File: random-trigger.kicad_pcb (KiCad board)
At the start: 2 copper layers, 50.5 x 100 mm, 70 parts, among them J1 Eurorack Power, J10 Trigger Out B, J11 Inv Trigger Out B, J2 Noise In, J3 Noise Out, J4 Trigger In A, J5 Gate Out A, J6 Trigger Out A, J7 Inv Trigger Out A, J8 Trigger In B, J9 Gate Out B, Q1 2N3904, Q2 2N3904, U1 TL074, U2 LM7805_TO220, U3 4013, U4 4081

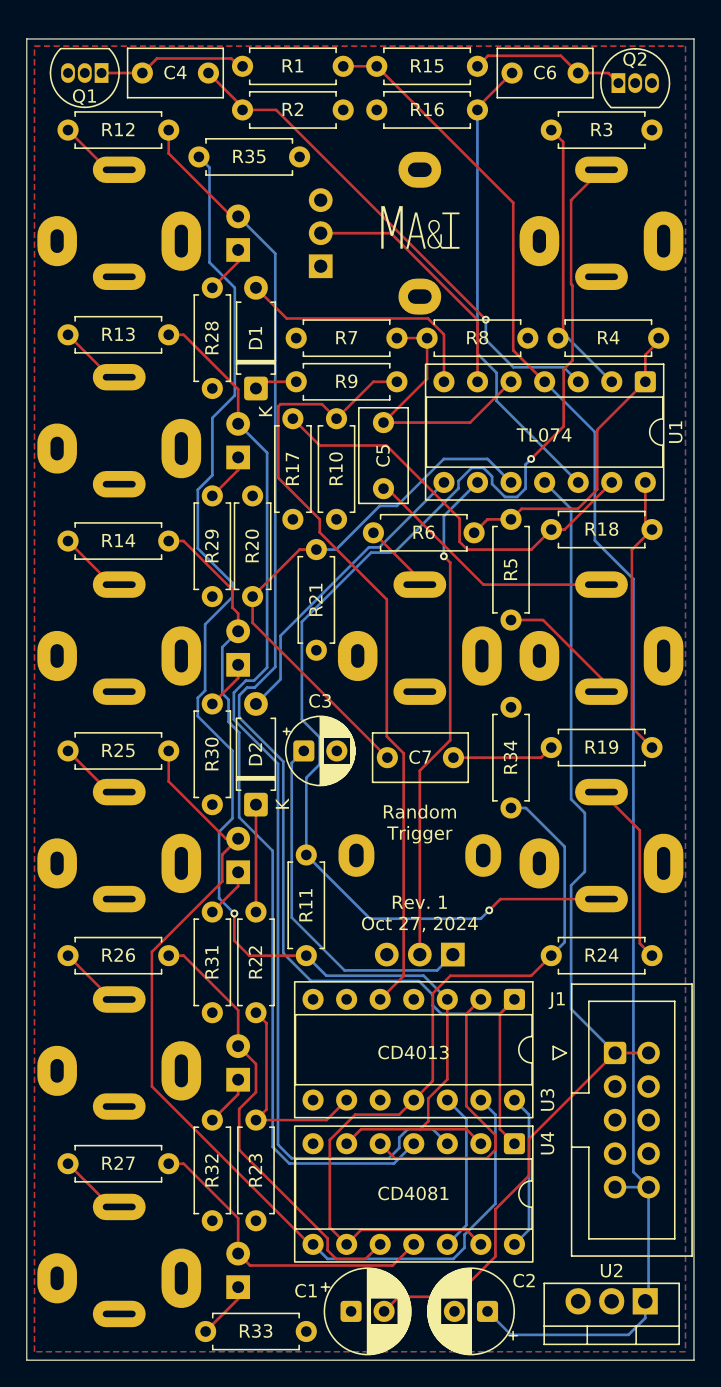
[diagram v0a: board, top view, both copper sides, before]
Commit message: Redo PCB to have all components on front
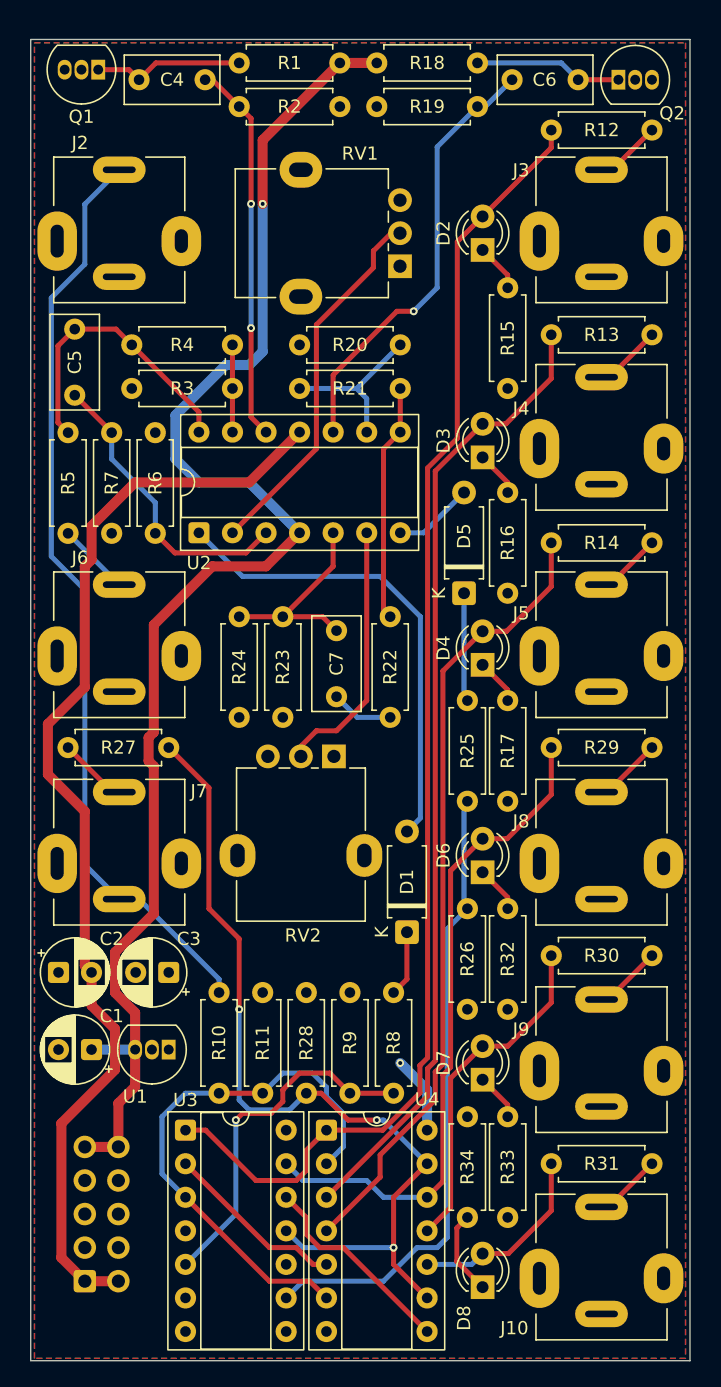
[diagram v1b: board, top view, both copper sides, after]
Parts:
- removed J11: Inv Trigger Out B, MAI_Connector_Audio:Jack_3.5mm_QingPu_WQP-PJ301BM_Vertical
- removed R35: 1M, Resistor_THT:R_Axial_DIN0207_L6.3mm_D2.5mm_P7.62mm_Horizontal
- removed the REF** at (129.8, 64.3)
- added REF**: Untitled, MAI_Logo:MAI_Logo_10mm_Silkscreen, B.Cu at (125.2, 83.6)
- C1, C2: footprint Capacitor_THT:CP_Radial_D6.3mm_P2.50mm -> Capacitor_THT:CP_Radial_D5.0mm_P2.50mm
- D2: value 1n4001 -> LED; footprint Diode_THT:D_A-405_P7.62mm_Horizontal -> LED_THT:LED_D3.0mm
- D3, D4, D6, D7, D8, RV1, RV2: moved to F.Cu
- D5: value LED -> 1n4001; footprint LED_THT:LED_D3.0mm -> Diode_THT:D_A-405_P7.62mm_Horizontal; moved to F.Cu
- J1: moved to B.Cu
- J10: value Trigger Out B -> Inv Trigger Out B; moved to F.Cu
- J2: value Noise In -> Trigger In A; moved to F.Cu
- J3: value Noise Out -> Gate Out A; moved to F.Cu
- J4: value Trigger In A -> Trigger Out A; moved to F.Cu
- J5: value Gate Out A -> Inv Trigger Out A; moved to F.Cu
- J6: value Trigger Out A -> Noise Out; moved to F.Cu
- J7: value Inv Trigger Out A -> Trigger In B; moved to F.Cu
- J8: value Trigger In B -> Gate Out B; moved to F.Cu
- J9: value Gate Out B -> Trigger Out B; moved to F.Cu
- R10, R22: value 1k5 -> 1k
- R11, R28: value 1k -> 1M
- R15, R16: value 100k -> 1k
- R17: value 330 -> 1k
- R18: value 1M -> 100k
- R19, R24, R6: value 1k -> 100k
- R20: value 100k -> 330
- R21: value 100k -> 1M
- R23: value 1k5 -> 100k
- R25, R26: value 1k -> 1k5
- R34: value 1M -> 1k
- R8: value 100k -> 1k5
- U1: value TL074 -> L78L05_TO92; footprint Package_DIP:DIP-14_W7.62mm_Socket -> Package_TO_SOT_THT:TO-92_Inline
- U2: value LM7805_TO220 -> TL074; footprint Package_TO_SOT_THT:TO-220-3_Vertical -> MAI_Package_DIP:DIP-14_W7.62mm_Socket_WithChip
- U3, U4: footprint Package_DIP:DIP-14_W7.62mm_Socket -> MAI_Package_DIP:DIP-14_W7.62mm_Socket_WithChip
- moved U2 67.3 mm to (113.0, 87.4), turned to 90 degrees
- moved U1 62.1 mm to (110.7, 126.5), turned to 180 degrees
- moved R28 61.4 mm to (121.2, 129.8), turned to 90 degrees
- moved R19 50.3 mm to (134.1, 55.1)
- moved R8 49.6 mm to (127.8, 122.2), turned to -90 degrees
- moved J2 48.1 mm to (107.0, 64.7), turned to 0 degrees
- moved J5 48.1 mm to (143.5, 96.1), turned to 0 degrees
- moved R9 46.4 mm to (124.5, 122.2), turned to -90 degrees
- moved D2 45.3 mm to (134.5, 66.0)
- moved R10 44.3 mm to (114.6, 129.8)
- moved J1 43.7 mm to (104.4, 144.0)
- moved D1 42.7 mm to (128.8, 117.6)
- moved C2 41.4 mm to (102.4, 120.7), turned to 0 degrees
- moved J9 39.7 mm to (143.5, 127.5), turned to 0 degrees
- moved J10 39.7 mm to (143.5, 143.2), turned to 0 degrees
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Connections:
- C1 pad 1: GND -> +12V
- C1 pad 2: -12V -> GND
- C2 pad 1: +12V -> GND
- C2 pad 2: GND -> -12V
- C4 pad 2: Net-(U1A-+) -> Net-(U2D-+)
- C5 pad 2: Net-(U1B-+) -> Net-(U2A-+)
- C6 pad 2: Net-(U1D-+) -> Net-(U2C-+)
- C7 pad 2: Net-(U1C-+) -> Net-(U2B-+)
- J2 pad T: Net-(C5-Pad1) -> Trigger Normal
- J2 pad TN: Net-(J2-PadTN) -> unconnected-(J2-PadTN)
- J4 pad T: Trigger Normal -> Net-(J4-PadT)
- J7 pad TN: unconnected-(J7-PadTN) -> Trigger Normal
- J8 pad TN: Trigger Normal -> unconnected-(J8-PadTN)
- R10 pad 1: GND -> Net-(U3A-C)
- R10 pad 2: Net-(U3A-D) -> Trigger Normal
- R11 pad 2: Trigger Normal -> GND
- R12 pad 1: Net-(D3-A) -> Net-(D2-A)
- R12 pad 2: Net-(J5-PadT) -> Net-(J3-PadT)
- R13 pad 1: Net-(D4-A) -> Net-(D3-A)
- R13 pad 2: Net-(J6-PadT) -> Net-(J4-PadT)
- R14 pad 1: Net-(D5-A) -> Net-(D4-A)
- R14 pad 2: Net-(J7-PadT) -> Net-(J5-PadT)
- R15 pad 1: +12V -> Net-(D2-K)
- R15 pad 2: Net-(Q2-E) -> GND
- R16 pad 1: Net-(U1D-+) -> Net-(D3-K)
- R17 pad 1: Net-(U1D--) -> Net-(D4-K)
- R18 pad 1: Net-(U1D--) -> +12V
- R18 pad 2: Net-(R18-Pad2) -> Net-(Q2-E)
- R19 pad 1: Net-(R18-Pad2) -> Net-(U2C-+)
- R19 pad 2: Net-(C7-Pad1) -> GND
- R2 pad 1: Net-(U1A-+) -> Net-(U2D-+)
- R20 pad 1: +5V -> Net-(U2C--)
- R20 pad 2: Net-(U1C-+) -> GND
- R21 pad 1: Net-(U1C-+) -> Net-(U2C--)
- R21 pad 2: GND -> Net-(R21-Pad2)
- R22 pad 1: Net-(D2-K) -> Net-(R21-Pad2)
- R22 pad 2: Net-(U3B-D) -> Net-(C7-Pad1)
- R23 pad 1: GND -> +5V
- R23 pad 2: Net-(U3B-D) -> Net-(U2B-+)
- R24 pad 1: Net-(U3B-C) -> Net-(U2B-+)
- R24 pad 2: Net-(J8-PadT) -> GND
- R25 pad 1: Net-(D6-A) -> Net-(D5-K)
- R25 pad 2: Net-(J9-PadT) -> Net-(U3B-D)
- R26 pad 1: Net-(D7-A) -> GND
- R26 pad 2: Net-(J10-PadT) -> Net-(U3B-D)
- R27 pad 1: Net-(D8-A) -> Net-(U3B-C)
- R27 pad 2: Net-(J11-PadT) -> Net-(J7-PadT)
- R28 pad 1: Net-(D3-K) -> Net-(U3B-C)
- R29 pad 1: Net-(D4-K) -> Net-(D6-A)
- R29 pad 2: GND -> Net-(J8-PadT)
- R3 pad 1: Net-(U1A--) -> Net-(U2D--)
- R30 pad 1: Net-(D5-K) -> Net-(D7-A)
- R30 pad 2: GND -> Net-(J9-PadT)
- R31 pad 1: Net-(D6-K) -> Net-(D8-A)
- R31 pad 2: GND -> Net-(J10-PadT)
- R32 pad 1: Net-(D7-K) -> Net-(D6-K)
- R33 pad 1: Net-(D8-K) -> Net-(D7-K)
- R34 pad 1: Net-(U3B-C) -> Net-(D8-K)
- R4 pad 1: Net-(U1A--) -> Net-(U2D--)
- R4 pad 2: Net-(R4-Pad2) -> Net-(C5-Pad1)
- R5 pad 1: Net-(R4-Pad2) -> Net-(C5-Pad1)
- R5 pad 2: Net-(J2-PadTN) -> Net-(J6-PadT)
- R6 pad 1: Net-(R4-Pad2) -> +5V
- R6 pad 2: Net-(J3-PadT) -> Net-(U2A-+)
- R7 pad 1: +5V -> Net-(U2A-+)
- R7 pad 2: Net-(U1B-+) -> GND
- R8 pad 1: Net-(U1B-+) -> Net-(D1-K)
- R8 pad 2: GND -> Net-(U3A-D)
- R9 pad 1: Net-(D1-K) -> GND
- RV1 pad 2: Net-(U1B--) -> Net-(U2A--)
- RV2 pad 2: Net-(U1C--) -> Net-(U2B--)
- U1 pad 1: Net-(R4-Pad2) -> +5V
- U1 pad 2: Net-(U1A--) -> GND
- U1 pad 3: Net-(U1A-+) -> +12V
- U2 pad 1: +12V -> Net-(D1-A)
- U2 pad 2: GND -> Net-(U2A--)
- U2 pad 3: +5V -> Net-(U2A-+)
- U3 pad 1: Net-(D3-A) -> Net-(D2-A)
- U4 pad 1: Net-(D3-A) -> Net-(D2-A)
- U4 pad 10: Net-(D7-A) -> Net-(D8-A)
- U4 pad 11: Net-(D8-A) -> Net-(D7-A)
- U4 pad 12: Net-(U3B-~{Q}) -> Net-(D6-A)
- U4 pad 3: Net-(D4-A) -> Net-(D3-A)
- U4 pad 4: Net-(D5-A) -> Net-(D4-A)
- U4 pad 8: Net-(D6-A) -> Net-(U3B-~{Q})
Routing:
- net Net-(D2-A): track 23.1 -> 100.0 mm
- net Net-(U3A-C): track 105.5 -> 41.8 mm, vias 1 -> 0
- net Net-(D5-A): track 62.6 -> 6.09 mm
- net Net-(U1C-+): track 41.0 -> 0.00 mm
- net Net-(U1A-+): track 38.7 -> 0.00 mm, vias 1 -> 0
- net Net-(U1C--): track 37.9 -> 0.00 mm, vias 1 -> 0
- net Net-(U1D-+): track 35.2 -> 0.00 mm
- net +5V: track 39.7 -> 5.92 mm, vias 0 -> 1
- net Net-(U2C-+): track 0.00 -> 33.4 mm, vias 0 -> 1
- net Net-(U3A-D): track 60.2 -> 27.1 mm, vias 0 -> 1
- net Net-(U3B-D): track 16.3 -> 47.9 mm
- net Net-(U1D--): track 31.4 -> 0.00 mm
- net Net-(U2D-+): track 0.00 -> 28.9 mm, vias 0 -> 2
- net Net-(U2A--): track 0.00 -> 28.3 mm
- net Net-(D3-A): track 100.9 -> 73.4 mm
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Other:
- board size 50.5 x 100 mm -> 49.9 x 100 mm
- board text added: "-12V STRIPE"
- board text added: "Random Trigger Rev. 2"
- board text removed: "CD4013"
- board text removed: "CD4081"
- board text removed: "Gate Out A"
- board text removed: "Gate Out B"
- board text removed: "Inv Out A"
- board text removed: "Inv Out B"
- board text removed: "Noise In"
- board text removed: "Noise Out"
- board text removed: "Probability A"
- board text removed: "Probability B"
- board text removed: "Random Trigger"
- board text removed: "Rev. 1 Oct 27, 2024"
- board text removed: "TL074"
- board text removed: "Trig In A"
- board text removed: "Trig In B"
- board text removed: "Trig Out A"
- board text removed: "Trig Out B"

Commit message: Use correct box capacitor footprint
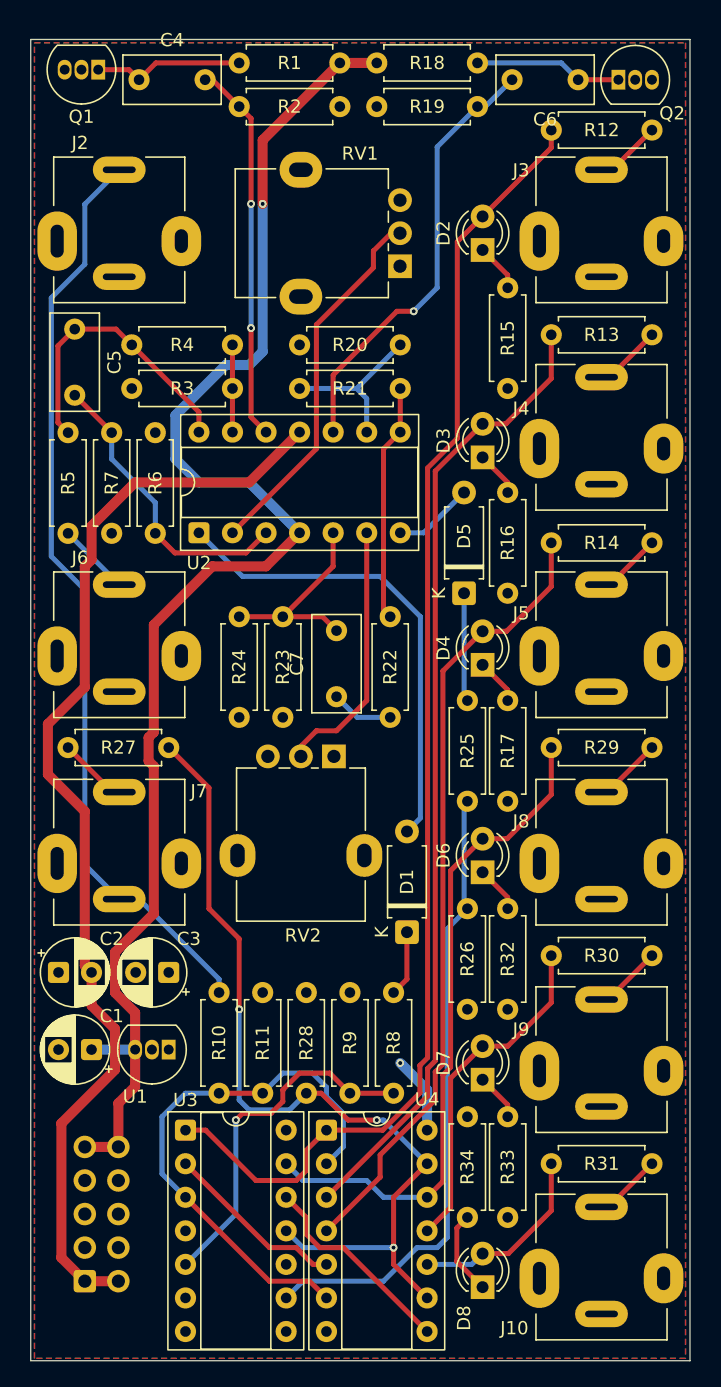
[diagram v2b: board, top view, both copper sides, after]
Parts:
- C4, C5, C6, C7: footprint Capacitor_THT:C_Rect_L7.0mm_W3.5mm_P5.00mm -> Capacitor_THT:C_Rect_L7.2mm_W3.5mm_P5.00mm_FKS2_FKP2_MKS2_MKP2
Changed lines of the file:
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@@
 		)
 	)
-	(footprint "Capacitor_THT:C_Rect_L7.0mm_W3.5mm_P5.00mm"
+	(footprint "Capacitor_THT:C_Rect_L7.2mm_W3.5mm_P5.00mm_FKS2_FKP2_MKS2_MKP2"
 		(layer "F.Cu")
 		(at 123.444 99.782 90)
-		(descr "C, Rect series, Radial, pin pitch=5.00mm, length*width=7*3.5mm^2, Capacitor")
-		(tags "C Rect series Radial pin pitch 5.00mm length 7mm width 3.5mm Capacitor")
+		(descr "C, Rect series, Radial, pin pitch=5.00mm, length*width=7.2*3.5mm^2, Capacitor, http://www.wima.com/EN/WIMA_FKS_2.pdf")
+		(tags "C Rect series Radial pin pitch 5.00mm length 7.2mm width 3.5mm Capacitor")
 		(property "Reference" "C7"
-			(at 2.5 0 90)
+			(at 2.5 -3 90)
 			(layer "F.SilkS")
 			(effects
@@
 		(attr through_hole)
 		(fp_line
-			(start 6.12 -1.87)
-			(end 6.12 1.87)
+			(start 6.22 -1.87)
+			(end 6.22 1.87)
 			(stroke
 				(width 0.12)
@@
 		)
 		(fp_line
-			(start -1.12 -1.87)
-			(end 6.12 -1.87)
+			(start -1.22 -1.87)
+			(end 6.22 -1.87)
 			(stroke
 				(width 0.12)
@@
 		)
 		(fp_line
-			(start 6.12 1.87)
-			(end -1.12 1.87)
+			(start 6.22 1.87)
+			(end -1.22 1.87)
 			(stroke
 				(width 0.12)
@@
 		)
 		(fp_line
-			(start -1.12 1.87)
-			(end -1.12 -1.87)
+			(start -1.22 1.87)
+			(end -1.22 -1.87)
 			(stroke
 				(width 0.12)
@@
 		)
 		(fp_rect
-			(start -1.25 -2)
-			(end 6.25 2)
+			(start -1.35 -2)
+			(end 6.35 2)
 			(stroke
 				(width 0.05)
@@
 		)
 		(fp_rect
-			(start -1 -1.75)
-			(end 6 1.75)
+			(start -1.1 -1.75)
+			(end 6.1 1.75)
 			(stroke
 				(width 0.1)
@@
 		)
 		(embedded_fonts no)
-		(model "${KICAD9_3DMODEL_DIR}/Capacitor_THT.3dshapes/C_Rect_L7.0mm_W3.5mm_P5.00mm.step"
+		(model "${KICAD9_3DMODEL_DIR}/Capacitor_THT.3dshapes/C_Rect_L7.2mm_W3.5mm_P5.00mm_FKS2_FKP2_MKS2_MKP2.step"
 			(offset
 				(xyz 0 0 0)
@@
 		)
 	)
-	(footprint "Capacitor_THT:C_Rect_L7.0mm_W3.5mm_P5.00mm"
+	(footprint "Capacitor_THT:C_Rect_L7.2mm_W3.5mm_P5.00mm_FKS2_FKP2_MKS2_MKP2"
 		(layer "F.Cu")
 		(at 108.498 53.086)
-		(descr "C, Rect series, Radial, pin pitch=5.00mm, length*width=7*3.5mm^2, Capacitor")
-		(tags "C Rect series Radial pin pitch 5.00mm length 7mm width 3.5mm Capacitor")
+		(descr "C, Rect series, Radial, pin pitch=5.00mm, length*width=7.2*3.5mm^2, Capacitor, http://www.wima.com/EN/WIMA_FKS_2.pdf")
+		(tags "C Rect series Radial pin pitch 5.00mm length 7.2mm width 3.5mm Capacitor")
 		(property "Reference" "C4"
-			(at 2.5 0 0)
+			(at 2.5 -3 0)
 			(layer "F.SilkS")
 			(effects
@@
 		(attr through_hole)
 		(fp_line
-			(start -1.12 -1.87)
-			(end 6.12 -1.87)
+			(start -1.22 -1.87)
+			(end 6.22 -1.87)
 			(stroke
 				(width 0.12)
@@
 		)
 		(fp_line
-			(start -1.12 1.87)
-			(end -1.12 -1.87)
+			(start -1.22 1.87)
+			(end -1.22 -1.87)
 			(stroke
 				(width 0.12)
@@
 		)
 		(fp_line
-			(start 6.12 -1.87)
-			(end 6.12 1.87)
+			(start 6.22 -1.87)
+			(end 6.22 1.87)
 			(stroke
 				(width 0.12)
@@
 		)
 		(fp_line
-			(start 6.12 1.87)
-			(end -1.12 1.87)
+			(start 6.22 1.87)
+			(end -1.22 1.87)
 			(stroke
 				(width 0.12)
@@
 		)
 		(fp_rect
-			(start -1.25 -2)
-			(end 6.25 2)
+			(start -1.35 -2)
+			(end 6.35 2)
 			(stroke
 				(width 0.05)
@@
 		)
 		(fp_rect
-			(start -1 -1.75)
-			(end 6 1.75)
+			(start -1.1 -1.75)
+			(end 6.1 1.75)
 			(stroke
 				(width 0.1)
@@
 		)
 		(embedded_fonts no)
-		(model "${KICAD9_3DMODEL_DIR}/Capacitor_THT.3dshapes/C_Rect_L7.0mm_W3.5mm_P5.00mm.step"
+		(model "${KICAD9_3DMODEL_DIR}/Capacitor_THT.3dshapes/C_Rect_L7.2mm_W3.5mm_P5.00mm_FKS2_FKP2_MKS2_MKP2.step"
 			(offset
 				(xyz 0 0 0)
@@
 		)
 	)
-	(footprint "Capacitor_THT:C_Rect_L7.0mm_W3.5mm_P5.00mm"
+	(footprint "Capacitor_THT:C_Rect_L7.2mm_W3.5mm_P5.00mm_FKS2_FKP2_MKS2_MKP2"
 		(layer "F.Cu")
 		(at 103.632 71.962 -90)
-		(descr "C, Rect series, Radial, pin pitch=5.00mm, length*width=7*3.5mm^2, Capacitor")
-		(tags "C Rect series Radial pin pitch 5.00mm length 7mm width 3.5mm Capacitor")
+		(descr "C, Rect series, Radial, pin pitch=5.00mm, length*width=7.2*3.5mm^2, Capacitor, http://www.wima.com/EN/WIMA_FKS_2.pdf")
+		(tags "C Rect series Radial pin pitch 5.00mm length 7.2mm width 3.5mm Capacitor")
 		(property "Reference" "C5"
-			(at 2.5 0 90)
+			(at 2.5 -3 270)
 			(layer "F.SilkS")
 			(effects
@@
 		)
 		(property "Value" "470n"
-			(at 2.5 3 90)
+			(at 2.5 3 270)
 			(layer "F.Fab")
 			(effects
@@
 		)
 		(property "Datasheet" "~"
-			(at 0 0 90)
+			(at 0 0 270)
 			(layer "F.Fab")
 			(hide yes)
@@
 		)
 		(property "Description" "Unpolarized capacitor"
-			(at 0 0 90)
+			(at 0 0 270)
 			(layer "F.Fab")
 			(hide yes)
@@
 		(attr through_hole)
 		(fp_line
-			(start -1.12 1.87)
-			(end -1.12 -1.87)
+			(start -1.22 1.87)
+			(end -1.22 -1.87)
 			(stroke
 				(width 0.12)
@@
 		)
 		(fp_line
-			(start 6.12 1.87)
-			(end -1.12 1.87)
+			(start 6.22 1.87)
+			(end -1.22 1.87)
 			(stroke
 				(width 0.12)
@@
 		)
 		(fp_line
-			(start -1.12 -1.87)
-			(end 6.12 -1.87)
+			(start -1.22 -1.87)
+			(end 6.22 -1.87)
 			(stroke
 				(width 0.12)
@@
 		)
 		(fp_line
-			(start 6.12 -1.87)
-			(end 6.12 1.87)
+			(start 6.22 -1.87)
+			(end 6.22 1.87)
 			(stroke
 				(width 0.12)
@@
 		)
 		(fp_rect
-			(start -1.25 -2)
-			(end 6.25 2)
+			(start -1.35 -2)
+			(end 6.35 2)
 			(stroke
 				(width 0.05)
@@
 		)
 		(fp_rect
-			(start -1 -1.75)
-			(end 6 1.75)
+			(start -1.1 -1.75)
+			(end 6.1 1.75)
 			(stroke
 				(width 0.1)
@@
 		)
 		(fp_text user "${REFERENCE}"
-			(at 2.5 0 90)
+			(at 2.5 0 270)
 			(layer "F.Fab")
 			(effects
@@
 		)
 		(embedded_fonts no)
-		(model "${KICAD9_3DMODEL_DIR}/Capacitor_THT.3dshapes/C_Rect_L7.0mm_W3.5mm_P5.00mm.step"
+		(model "${KICAD9_3DMODEL_DIR}/Capacitor_THT.3dshapes/C_Rect_L7.2mm_W3.5mm_P5.00mm_FKS2_FKP2_MKS2_MKP2.step"
 			(offset
 				(xyz 0 0 0)
@@
 		)
 	)
-	(footprint "Capacitor_THT:C_Rect_L7.0mm_W3.5mm_P5.00mm"
+	(footprint "Capacitor_THT:C_Rect_L7.2mm_W3.5mm_P5.00mm_FKS2_FKP2_MKS2_MKP2"
 		(layer "F.Cu")
 		(at 141.732 53.086 180)
-		(descr "C, Rect series, Radial, pin pitch=5.00mm, length*width=7*3.5mm^2, Capacitor")
-		(tags "C Rect series Radial pin pitch 5.00mm length 7mm width 3.5mm Capacitor")
+		(descr "C, Rect series, Radial, pin pitch=5.00mm, length*width=7.2*3.5mm^2, Capacitor, http://www.wima.com/EN/WIMA_FKS_2.pdf")
+		(tags "C Rect series Radial pin pitch 5.00mm length 7.2mm width 3.5mm Capacitor")
 		(property "Reference" "C6"
-			(at 2.54 0 0)
+			(at 2.5 -3 180)
 			(layer "F.SilkS")
 			(effects
@@
 		)
 		(property "Value" "470n"
-			(at 2.5 3 0)
+			(at 2.5 3 180)
 			(layer "F.Fab")
 			(effects
@@
 		)
 		(property "Datasheet" "~"
-			(at 0 0 0)
+			(at 0 0 180)
 			(layer "F.Fab")
 			(hide yes)
@@
 		)
 		(property "Description" "Unpolarized capacitor"
-			(at 0 0 0)
+			(at 0 0 180)
 			(layer "F.Fab")
 			(hide yes)
@@
 		(attr through_hole)
 		(fp_line
-			(start 6.12 1.87)
-			(end -1.12 1.87)
+			(start 6.22 1.87)
+			(end -1.22 1.87)
 			(stroke
 				(width 0.12)
@@
 		)
 		(fp_line
-			(start 6.12 -1.87)
-			(end 6.12 1.87)
+			(start 6.22 -1.87)
+			(end 6.22 1.87)
 			(stroke
 				(width 0.12)
@@
 		)
 		(fp_line
-			(start -1.12 1.87)
-			(end -1.12 -1.87)
+			(start -1.22 1.87)
+			(end -1.22 -1.87)
 			(stroke
 				(width 0.12)
@@
 		)
 		(fp_line
-			(start -1.12 -1.87)
-			(end 6.12 -1.87)
+			(start -1.22 -1.87)
+			(end 6.22 -1.87)
 			(stroke
 				(width 0.12)
@@
 		)
 		(fp_rect
-			(start -1.25 -2)
-			(end 6.25 2)
+			(start -1.35 -2)
+			(end 6.35 2)
 			(stroke
 				(width 0.05)
@@
 		)
 		(fp_rect
-			(start -1 -1.75)
-			(end 6 1.75)
+			(start -1.1 -1.75)
+			(end 6.1 1.75)
 			(stroke
 				(width 0.1)
@@
 		)
 		(fp_text user "${REFERENCE}"
-			(at 2.5 0 0)
+			(at 2.5 0 180)
 			(layer "F.Fab")
 			(effects
@@
 		)
 		(embedded_fonts no)
-		(model "${KICAD9_3DMODEL_DIR}/Capacitor_THT.3dshapes/C_Rect_L7.0mm_W3.5mm_P5.00mm.step"
+		(model "${KICAD9_3DMODEL_DIR}/Capacitor_THT.3dshapes/C_Rect_L7.2mm_W3.5mm_P5.00mm_FKS2_FKP2_MKS2_MKP2.step"
 			(offset
 				(xyz 0 0 0)
